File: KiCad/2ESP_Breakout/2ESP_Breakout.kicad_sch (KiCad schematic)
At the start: 36 parts, among them J1 Conn_01x15_Socket, J10 Conn_01x02_Socket, J11 Conn_01x02_Socket, J12 Conn_01x02_Socket, J13 Conn_01x02_Socket, J14 Conn_01x02_Socket, J15 Conn_01x02_Socket, J16 Conn_01x02_Socket, J17 Conn_01x02_Socket, J18 Conn_01x02_Socket, J19 Conn_01x02_Socket, J2 Conn_01x15_Socket, J20 Conn_01x02_Socket, J21 Conn_01x02_Socket, J22 Conn_01x02_Socket, J24 Conn_01x02_Socket, J26 Conn_01x02_Socket, J3 Conn_01x15_Socket, J4 Conn_01x15_Socket, J5 Conn_01x15_Socket, J6 Conn_01x15_Socket, J7 Conn_01x15_Socket, J8 Conn_01x15_Socket, J9 Conn_01x02_Socket

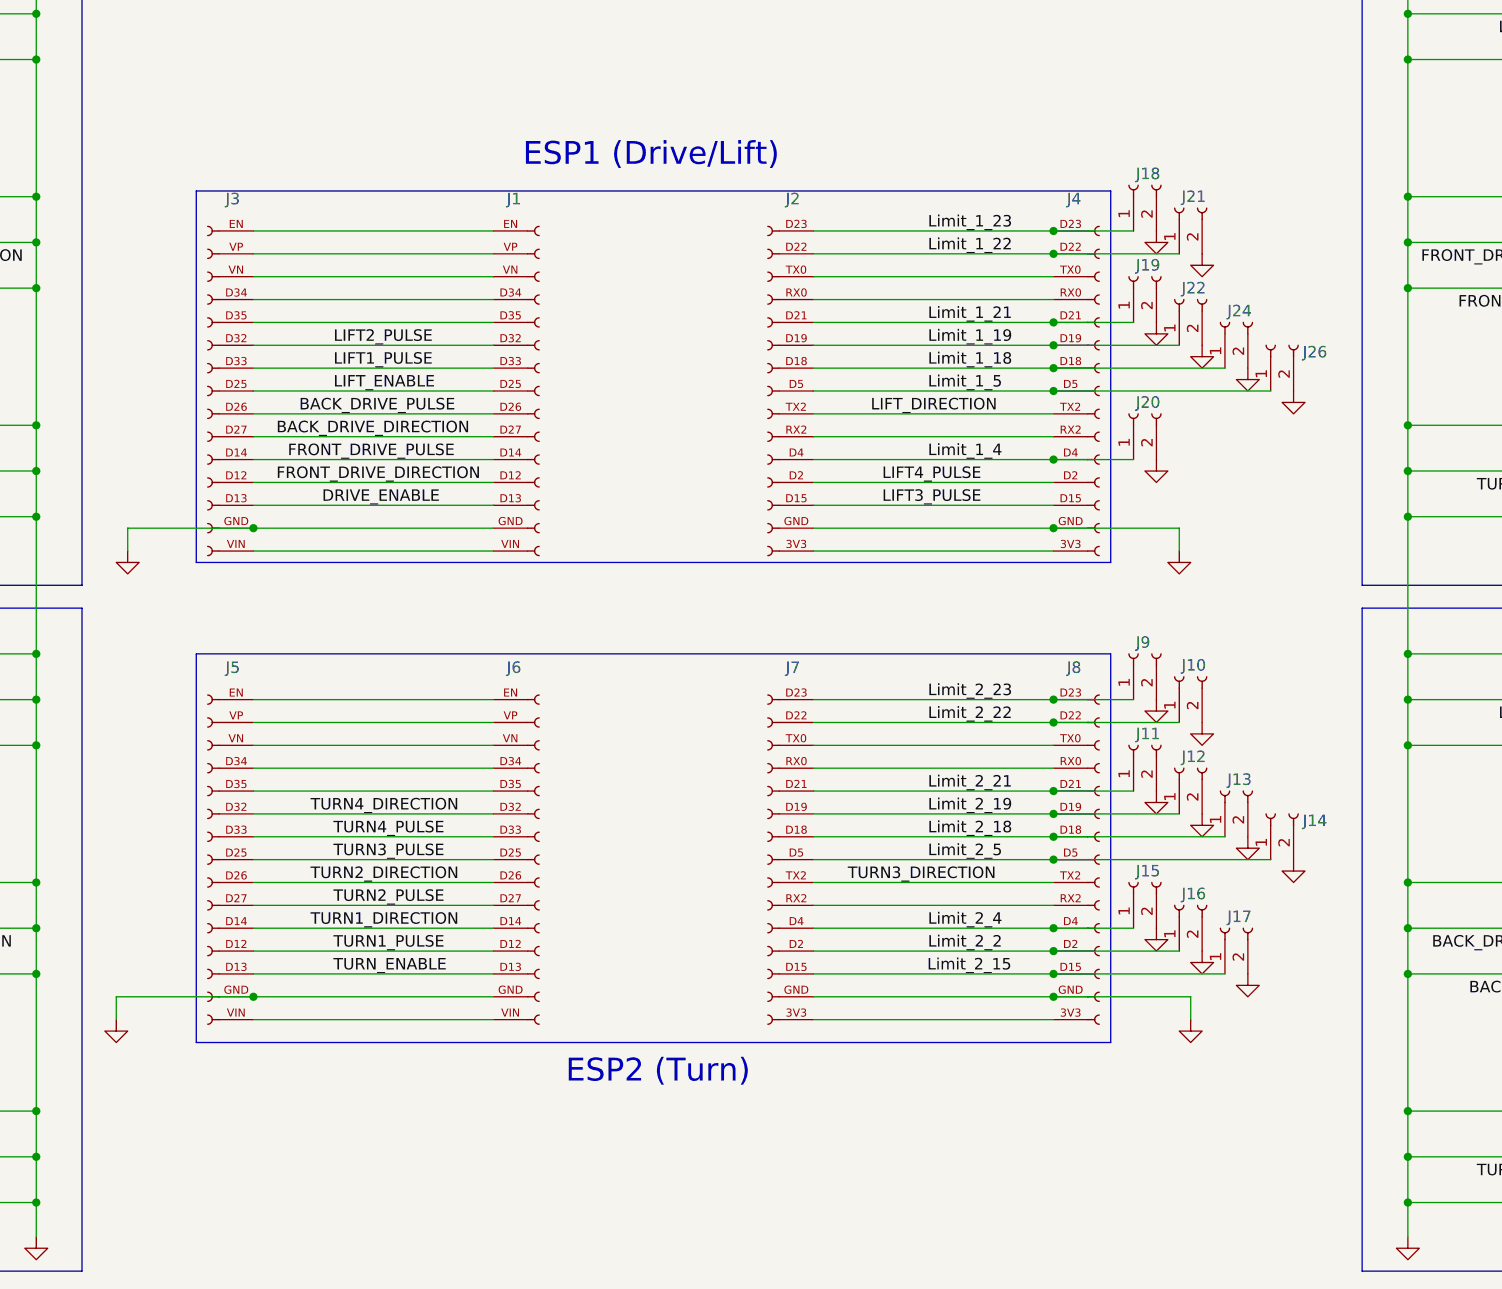
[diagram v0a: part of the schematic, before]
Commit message: Did some initial routing on breakout2
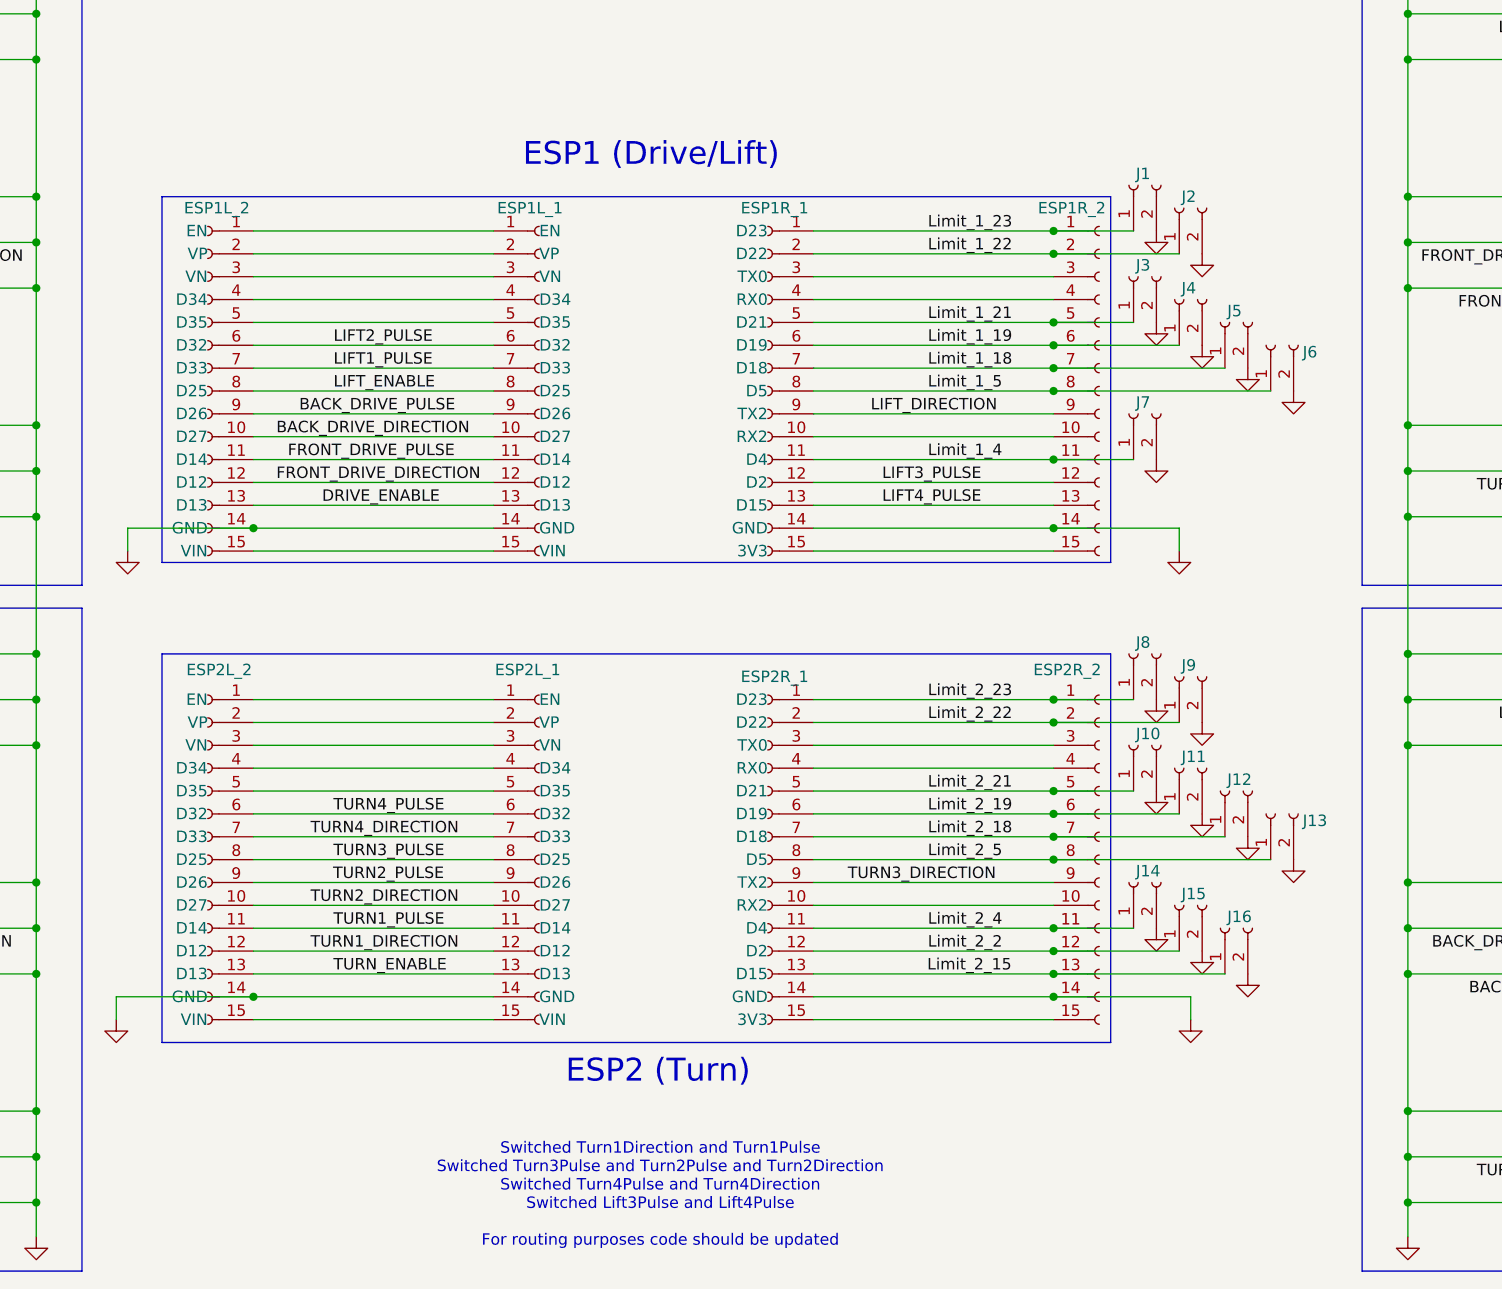
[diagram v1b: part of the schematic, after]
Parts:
- removed J3, J4, J5, J7, J8: Conn_01x15_Socket, Connector_PinSocket_2.54mm:PinSocket_1x15_P2.54mm_Vertical, symbol Connector:Conn_01x15_Socket
- added ESP1L_2, ESP2L_2: Conn_01x15_Socket, Connector_PinSocket_2.54mm:PinSocket_1x15_P2.54mm_Vertical, symbol ESP32_DevKitV1_Headers_Local:ESP32_DevKitV1_Header_LEFT
- added ESP1R_2, ESP2R_1, ESP2R_2: Conn_01x15_Socket, Connector_PinSocket_2.54mm:PinSocket_1x15_P2.54mm_Vertical, symbol ESP32_DevKitV1_Headers_Local:ESP32_DevKitV1_Header_RIGHT
- ESP1L_1: renamed from J1; symbol Connector:Conn_01x15_Socket -> ESP32_DevKitV1_Headers_Local:ESP32_DevKitV1_Header_LEFT
- ESP1R_1: renamed from J2; symbol Connector:Conn_01x15_Socket -> ESP32_DevKitV1_Headers_Local:ESP32_DevKitV1_Header_RIGHT
- ESP2L_1: renamed from J6; symbol Connector:Conn_01x15_Socket -> ESP32_DevKitV1_Headers_Local:ESP32_DevKitV1_Header_LEFT
- J1: renamed from J18; footprint (none) -> Connector_JST:JST_PH_B2B-PH-K_1x02_P2.00mm_Vertical
- J10: renamed from J11; footprint (none) -> Connector_JST:JST_PH_B2B-PH-K_1x02_P2.00mm_Vertical
- J11: renamed from J12; footprint (none) -> Connector_JST:JST_PH_B2B-PH-K_1x02_P2.00mm_Vertical
- J12: renamed from J13; footprint (none) -> Connector_JST:JST_PH_B2B-PH-K_1x02_P2.00mm_Vertical
- J13: renamed from J14; footprint (none) -> Connector_JST:JST_PH_B2B-PH-K_1x02_P2.00mm_Vertical
- J14: renamed from J15; footprint (none) -> Connector_JST:JST_PH_B2B-PH-K_1x02_P2.00mm_Vertical
- J15: renamed from J16; footprint (none) -> Connector_JST:JST_PH_B2B-PH-K_1x02_P2.00mm_Vertical
- J16: renamed from J17; footprint (none) -> Connector_JST:JST_PH_B2B-PH-K_1x02_P2.00mm_Vertical
- J2: renamed from J21; footprint (none) -> Connector_JST:JST_PH_B2B-PH-K_1x02_P2.00mm_Vertical
- J3: renamed from J19; footprint (none) -> Connector_JST:JST_PH_B2B-PH-K_1x02_P2.00mm_Vertical
- J4: renamed from J22; footprint (none) -> Connector_JST:JST_PH_B2B-PH-K_1x02_P2.00mm_Vertical
- J5: renamed from J24; footprint (none) -> Connector_JST:JST_PH_B2B-PH-K_1x02_P2.00mm_Vertical
- J6: renamed from J26; footprint (none) -> Connector_JST:JST_PH_B2B-PH-K_1x02_P2.00mm_Vertical
- J7: renamed from J20; footprint (none) -> Connector_JST:JST_PH_B2B-PH-K_1x02_P2.00mm_Vertical
- J8: renamed from J9; footprint (none) -> Connector_JST:JST_PH_B2B-PH-K_1x02_P2.00mm_Vertical
- J9: renamed from J10; footprint (none) -> Connector_JST:JST_PH_B2B-PH-K_1x02_P2.00mm_Vertical
- LIFT1, LIFT3, LIFT4, TURN1, TURN2, TURN3, TURN4: footprint Connector_JST:JST_PH_S6B-PH-K_1x06_P2.00mm_Horizontal -> Connector_JST:JST_PH_B6B-PH-K_1x06_P2.00mm_Vertical
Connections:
- net BACK_DRIVE_DIRECTION: now also ESP1L_1.10 (D27), ESP1L_2.10 (D27); no longer ESP1L_1.D27 (Pin_10)
- net BACK_DRIVE_PULSE: now also ESP1L_1.9 (D26), ESP1L_2.9 (D26); no longer ESP1L_1.D26 (Pin_9)
- net DRIVE_ENABLE: now also ESP1L_1.13 (D13), ESP1L_2.13 (D13); no longer ESP1L_1.D13 (Pin_13)
- net FRONT_DRIVE_DIRECTION: now also ESP1L_1.12 (D12), ESP1L_2.12 (D12); no longer ESP1L_1.D12 (Pin_12)
- net FRONT_DRIVE_PULSE: now also ESP1L_1.11 (D14), ESP1L_2.11 (D14); no longer ESP1L_1.D14 (Pin_11)
- net GND: now also ESP1L_1.14 (GND), ESP1R_1.14 (GND), ESP2L_1.14 (GND), ESP1L_2.14 (GND), ESP1R_2.14 (GND), ESP2L_2.14 (GND), ESP2R_1.14 (GND), ESP2R_2.14 (GND); no longer ESP1L_1.GND (Pin_14), ESP1R_1.GND (Pin_14), ESP2L_1.GND (Pin_14)
- net LIFT1_PULSE: now also ESP1L_1.7 (D33), ESP1L_2.7 (D33); no longer ESP1L_1.D33 (Pin_7)
- net LIFT2_PULSE: now also ESP1L_1.6 (D32), ESP1L_2.6 (D32); no longer ESP1L_1.D32 (Pin_6)
- net LIFT3_PULSE: now also ESP1R_1.12 (D2), ESP1R_2.12 (D2); no longer ESP1R_1.D15 (Pin_13)
- net LIFT4_PULSE: now also ESP1R_1.13 (D15), ESP1R_2.13 (D15); no longer ESP1R_1.D2 (Pin_12)
- net LIFT_DIRECTION: now also ESP1R_1.9 (TX2), ESP1R_2.9 (TX2); no longer ESP1R_1.TX2 (Pin_9)
- net LIFT_ENABLE: now also ESP1L_1.8 (D25), ESP1L_2.8 (D25); no longer ESP1L_1.D25 (Pin_8)
- net Limit_1_18: now also ESP1R_1.7 (D18), ESP1R_2.7 (D18); no longer ESP1R_1.D18 (Pin_7)
- net Limit_1_19: now also ESP1R_1.6 (D19), ESP1R_2.6 (D19); no longer ESP1R_1.D19 (Pin_6)
- net Limit_1_21: now also ESP1R_1.5 (D21), ESP1R_2.5 (D21); no longer ESP1R_1.D21 (Pin_5)
- net Limit_1_22: now also ESP1R_1.2 (D22), ESP1R_2.2 (D22); no longer ESP1R_1.D22 (Pin_2)
- net Limit_1_23: now also ESP1R_1.1 (D23), ESP1R_2.1 (D23); no longer ESP1R_1.D23 (Pin_1)
- net Limit_1_4: now also ESP1R_1.11 (D4), ESP1R_2.11 (D4); no longer ESP1R_1.D4 (Pin_11)
- net Limit_1_5: now also ESP1R_1.8 (D5), ESP1R_2.8 (D5); no longer ESP1R_1.D5 (Pin_8)
- net Limit_2_15: now also ESP2R_1.13 (D15), ESP2R_2.13 (D15)
- net Limit_2_18: now also ESP2R_1.7 (D18), ESP2R_2.7 (D18)
- net Limit_2_19: now also ESP2R_1.6 (D19), ESP2R_2.6 (D19)
- net Limit_2_2: now also ESP2R_1.12 (D2), ESP2R_2.12 (D2)
- net Limit_2_21: now also ESP2R_1.5 (D21), ESP2R_2.5 (D21)
- net Limit_2_22: now also ESP2R_1.2 (D22), ESP2R_2.2 (D22)
- net Limit_2_23: now also ESP2R_1.1 (D23), ESP2R_2.1 (D23)
- net Limit_2_4: now also ESP2R_1.11 (D4), ESP2R_2.11 (D4)
- net Limit_2_5: now also ESP2R_1.8 (D5), ESP2R_2.8 (D5)
- net TURN1_DIRECTION: now also ESP2L_1.12 (D12), ESP2L_2.12 (D12); no longer ESP2L_1.D14 (Pin_11)
- net TURN1_PULSE: now also ESP2L_1.11 (D14), ESP2L_2.11 (D14); no longer ESP2L_1.D12 (Pin_12)
- net TURN2_DIRECTION: now also ESP2L_1.10 (D27), ESP2L_2.10 (D27); no longer ESP2L_1.D26 (Pin_9)
- net TURN2_PULSE: now also ESP2L_1.9 (D26), ESP2L_2.9 (D26); no longer ESP2L_1.D27 (Pin_10)
- net TURN3_DIRECTION: now also ESP2R_1.9 (TX2), ESP2R_2.9 (TX2)
- net TURN3_PULSE: now also ESP2L_1.8 (D25), ESP2L_2.8 (D25); no longer ESP2L_1.D25 (Pin_8)
- net TURN4_DIRECTION: now also ESP2L_1.7 (D33), ESP2L_2.7 (D33); no longer ESP2L_1.D32 (Pin_6)
- net TURN4_PULSE: now also ESP2L_1.6 (D32), ESP2L_2.6 (D32); no longer ESP2L_1.D33 (Pin_7)
- net TURN_ENABLE: now also ESP2L_1.13 (D13), ESP2L_2.13 (D13); no longer ESP2L_1.D13 (Pin_13)
- new net: ESP2L_1.1 (EN), ESP2L_2.1 (EN)
- new net: ESP2L_1.15 (VIN), ESP2L_2.15 (VIN)
- new net: ESP2L_1.2 (VP), ESP2L_2.2 (VP)
- new net: ESP2L_1.3 (VN), ESP2L_2.3 (VN)
- new net: ESP2L_1.4 (D34), ESP2L_2.4 (D34)
- new net: ESP2L_1.5 (D35), ESP2L_2.5 (D35)
- new net: ESP2R_1.10 (RX2), ESP2R_2.10 (RX2)
- new net: ESP2R_1.15 (3V3), ESP2R_2.15 (3V3)
- new net: ESP2R_1.3 (TX0), ESP2R_2.3 (TX0)
- new net: ESP2R_1.4 (RX0), ESP2R_2.4 (RX0)
- new net: ESP1L_1.1 (EN), ESP1L_2.1 (EN)
- new net: ESP1L_1.15 (VIN), ESP1L_2.15 (VIN)
- new net: ESP1L_1.2 (VP), ESP1L_2.2 (VP)
- new net: ESP1L_1.3 (VN), ESP1L_2.3 (VN)
- new net: ESP1L_1.4 (D34), ESP1L_2.4 (D34)
- new net: ESP1L_1.5 (D35), ESP1L_2.5 (D35)
- new net: ESP1R_1.10 (RX2), ESP1R_2.10 (RX2)
- new net: ESP1R_1.15 (3V3), ESP1R_2.15 (3V3)
- new net: ESP1R_1.3 (TX0), ESP1R_2.3 (TX0)
- new net: ESP1R_1.4 (RX0), ESP1R_2.4 (RX0)
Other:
- note added: "Switched Turn1Direction and Turn1Pulse Switched Turn3Pulse and Turn2Pulse and Turn2Direction Switched Turn4Pulse and Turn4Direction Switched Lift3Pulse and Lift4Pulse For routing purposes code should be updated"

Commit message: Cleaned up routing
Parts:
- added Buck_Header1: Conn_01x04_Pin, Connector_PinHeader_2.54mm:PinHeader_1x04_P2.54mm_Vertical, symbol Connector:Conn_01x04_Pin
- added H1, H2, H3, H4: MountingHole, MountingHole:MountingHole_3.2mm_M3, symbol Mechanical:MountingHole
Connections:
- net GND: now also Buck_Header1.1 (Pin_1)
- net LIFT1_PULSE: now also ESP1R_1.6 (D19), ESP1R_2.6 (D19); no longer ESP1L_1.7 (D33), ESP1L_2.7 (D33)
- net LIFT2_PULSE: now also ESP1R_1.5 (D21), ESP1R_2.5 (D21); no longer ESP1L_1.6 (D32), ESP1L_2.6 (D32)
- net LIFT_ENABLE: now also ESP1R_1.7 (D18), ESP1R_2.7 (D18); no longer ESP1L_1.8 (D25), ESP1L_2.8 (D25)
- net TURN2_DIRECTION: now also ESP2L_1.8 (D25), ESP2L_2.8 (D25); no longer ESP2L_1.10 (D27), ESP2L_2.10 (D27)
- net TURN2_PULSE: now also ESP2L_1.7 (D33), ESP2L_2.7 (D33); no longer ESP2L_1.9 (D26), ESP2L_2.9 (D26)
- net TURN3_PULSE: now also ESP2L_1.6 (D32), ESP2L_2.6 (D32); no longer ESP2L_1.8 (D25), ESP2L_2.8 (D25)
- net TURN4_DIRECTION: now also ESP2L_1.10 (D27), ESP2L_2.10 (D27); no longer ESP2L_1.7 (D33), ESP2L_2.7 (D33)
- net TURN4_PULSE: now also ESP2L_1.9 (D26), ESP2L_2.9 (D26); no longer ESP2L_1.6 (D32), ESP2L_2.6 (D32)
- net at ESP2L_1.15 (VIN), ESP2L_2.15 (VIN): now also ESP1L_1.15 (VIN), ESP1L_2.15 (VIN), Buck_Header1.4 (Pin_4)
- removed net Limit_1_18: ESP1R_1.7 (D18), ESP1R_2.7 (D18), J5.1 (Pin_1)
- removed net Limit_1_19: ESP1R_1.6 (D19), ESP1R_2.6 (D19), J4.1 (Pin_1)
- removed net Limit_1_21: ESP1R_1.5 (D21), ESP1R_2.5 (D21), J3.1 (Pin_1)
- new net Limit_1_25: ESP1L_1.8 (D25), ESP1L_2.8 (D25), J5.1 (Pin_1)
- new net Limit_1_32: ESP1L_1.6 (D32), ESP1L_2.6 (D32), J3.1 (Pin_1)
- new net Limit_1_33: ESP1L_1.7 (D33), ESP1L_2.7 (D33), J4.1 (Pin_1)
- no-connect marks 0 -> 2
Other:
- moved on the sheet: DRIVE1, DRIVE3, J3, J4, J5, LIFT1, LIFT3, TURN1, TURN3

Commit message: Needs some more work on 2esp
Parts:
- removed J1, J8: Conn_01x02_Socket, Connector_JST:JST_PH_B2B-PH-K_1x02_P2.00mm_Vertical, symbol Connector:Conn_01x02_Socket
- added ESP3L1: Conn_01x15_Socket, Connector_PinSocket_2.54mm:PinSocket_1x15_P2.54mm_Vertical, symbol ESP32_DevKitV1_Headers_Local:ESP32_DevKitV1_Header_LEFT
- added ESP3R1: Conn_01x15_Socket, Connector_PinSocket_2.54mm:PinSocket_1x15_P2.54mm_Vertical, symbol ESP32_DevKitV1_Headers_Local:ESP32_DevKitV1_Header_RIGHT
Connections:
- net Limit_1_23 is gone; now on net LIFT_DIRECTION: ESP1R_1.1 (D23), ESP1R_2.1 (D23)
- net Limit_2_23 is gone; now on net TURN3_DIRECTION: ESP2R_1.1 (D23), ESP2R_2.1 (D23)
- net GND: now also ESP3L1.14 (GND), ESP3R1.14 (GND)
- net LIFT_DIRECTION: no longer ESP1R_1.9 (TX2), ESP1R_2.9 (TX2)
- net TURN3_DIRECTION: no longer ESP2R_1.9 (TX2), ESP2R_2.9 (TX2)
- net at Buck_Header1.4 (Pin_4), ESP1L_1.15 (VIN), ESP1L_2.15 (VIN)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: now also ESP3L1.15 (VIN)
- net TX_PARENT: now reaches ESP2R_1.10 (RX2), ESP2R_2.10 (RX2)
- net TX_PARENT: now also ESP1R_1.10 (RX2), ESP1R_2.10 (RX2), ESP3R1.9 (TX2)
- new net TX_CHILD1: ESP1R_1.9 (TX2), ESP1R_2.9 (TX2), ESP3R1.7 (D18)
- new net TX_CHILD2: ESP2R_1.9 (TX2), ESP2R_2.9 (TX2), ESP3R1.10 (RX2)
- no-connect marks 2 -> 26

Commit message: Final KiCad stuff for 2ESP and Driver Board
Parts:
- added ESP3L_2, ESP3L_3: Conn_01x15_Socket, Connector_PinSocket_2.54mm:PinSocket_1x15_P2.54mm_Vertical, symbol ESP32_DevKitV1_Headers_Local:ESP32_DevKitV1_Header_LEFT
- renumbered ESP3L1 to ESP3L_1, ESP3R1 to ESP3R_1
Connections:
- net GND: now also ESP3L_2.14 (GND), ESP3L_3.14 (GND)
- net TX_CHILD1: now also ESP3L_3.7 (D33)
- net TX_CHILD2: now also ESP3L_3.10 (D27)
- net 5V: now reaches Buck_Header1.4 (Pin_4), ESP1L_1.15 (VIN), ESP1L_2.15 (VIN), ESP2L_1.15 (VIN), ESP2L_2.15 (VIN), ESP3L_1.15 (VIN)
- net 5V: now also ESP3L_2.15 (VIN)
- net at ESP3L_1.1 (EN): now also ESP3L_2.1 (EN)
- net at ESP3L_1.10 (D27): now also ESP3L_2.10 (D27)
- net at ESP3L_1.11 (D14): now also ESP3L_2.11 (D14)
- net at ESP3L_1.12 (D12): now also ESP3L_2.12 (D12)
- net at ESP3L_1.13 (D13): now also ESP3L_2.13 (D13)
- net at ESP3L_1.2 (VP): now also ESP3L_2.2 (VP)
- net at ESP3L_1.3 (VN): now also ESP3L_2.3 (VN)
- net at ESP3L_1.4 (D34): now also ESP3L_2.4 (D34)
- net at ESP3L_1.5 (D35): now also ESP3L_2.5 (D35)
- net at ESP3L_1.6 (D32): now also ESP3L_2.6 (D32)
- net at ESP3L_1.7 (D33): now also ESP3L_2.7 (D33)
- net at ESP3L_1.8 (D25): now also ESP3L_2.8 (D25)
- net at ESP3L_1.9 (D26): now also ESP3L_2.9 (D26)
- net at ESP3R_1.1 (D23): now also ESP3L_3.1 (EN)
- net at ESP3R_1.11 (D4): now also ESP3L_3.11 (D14)
- net at ESP3R_1.12 (D2): now also ESP3L_3.12 (D12)
- net at ESP3R_1.13 (D15): now also ESP3L_3.13 (D13)
- net at ESP3R_1.15 (3V3): now also ESP3L_3.15 (VIN)
- net at ESP3R_1.2 (D22): now also ESP3L_3.2 (VP)
- net at ESP3R_1.3 (TX0): now also ESP3L_3.3 (VN)
- net at ESP3R_1.4 (RX0): now also ESP3L_3.4 (D34)
- net at ESP3R_1.5 (D21): now also ESP3L_3.5 (D35)
- net at ESP3R_1.6 (D19): now also ESP3L_3.6 (D32)
- net TX_PARENT1: now reaches ESP3R_1.8 (D5)
- net TX_PARENT1: now also ESP1R_1.10 (RX2), ESP1R_2.10 (RX2), ESP3L_3.8 (D25)
- net TX_PARENT renamed TX_PARENT2
- net TX_PARENT2: now also ESP3L_3.9 (D26); no longer ESP1R_1.10 (RX2), ESP1R_2.10 (RX2)
- no-connect marks 26 -> 2
